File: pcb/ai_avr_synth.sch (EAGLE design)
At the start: 45 parts, among them IC1 ATMEGA328P-PDIP, J1 1X02ST, J2 1X06, J3 1X08, J4 1X08, J5 MIDIJACK, J6 STEREOJACKSJ1-3555NG, U1 MC7805, U2 TLC2262, U3 6N138

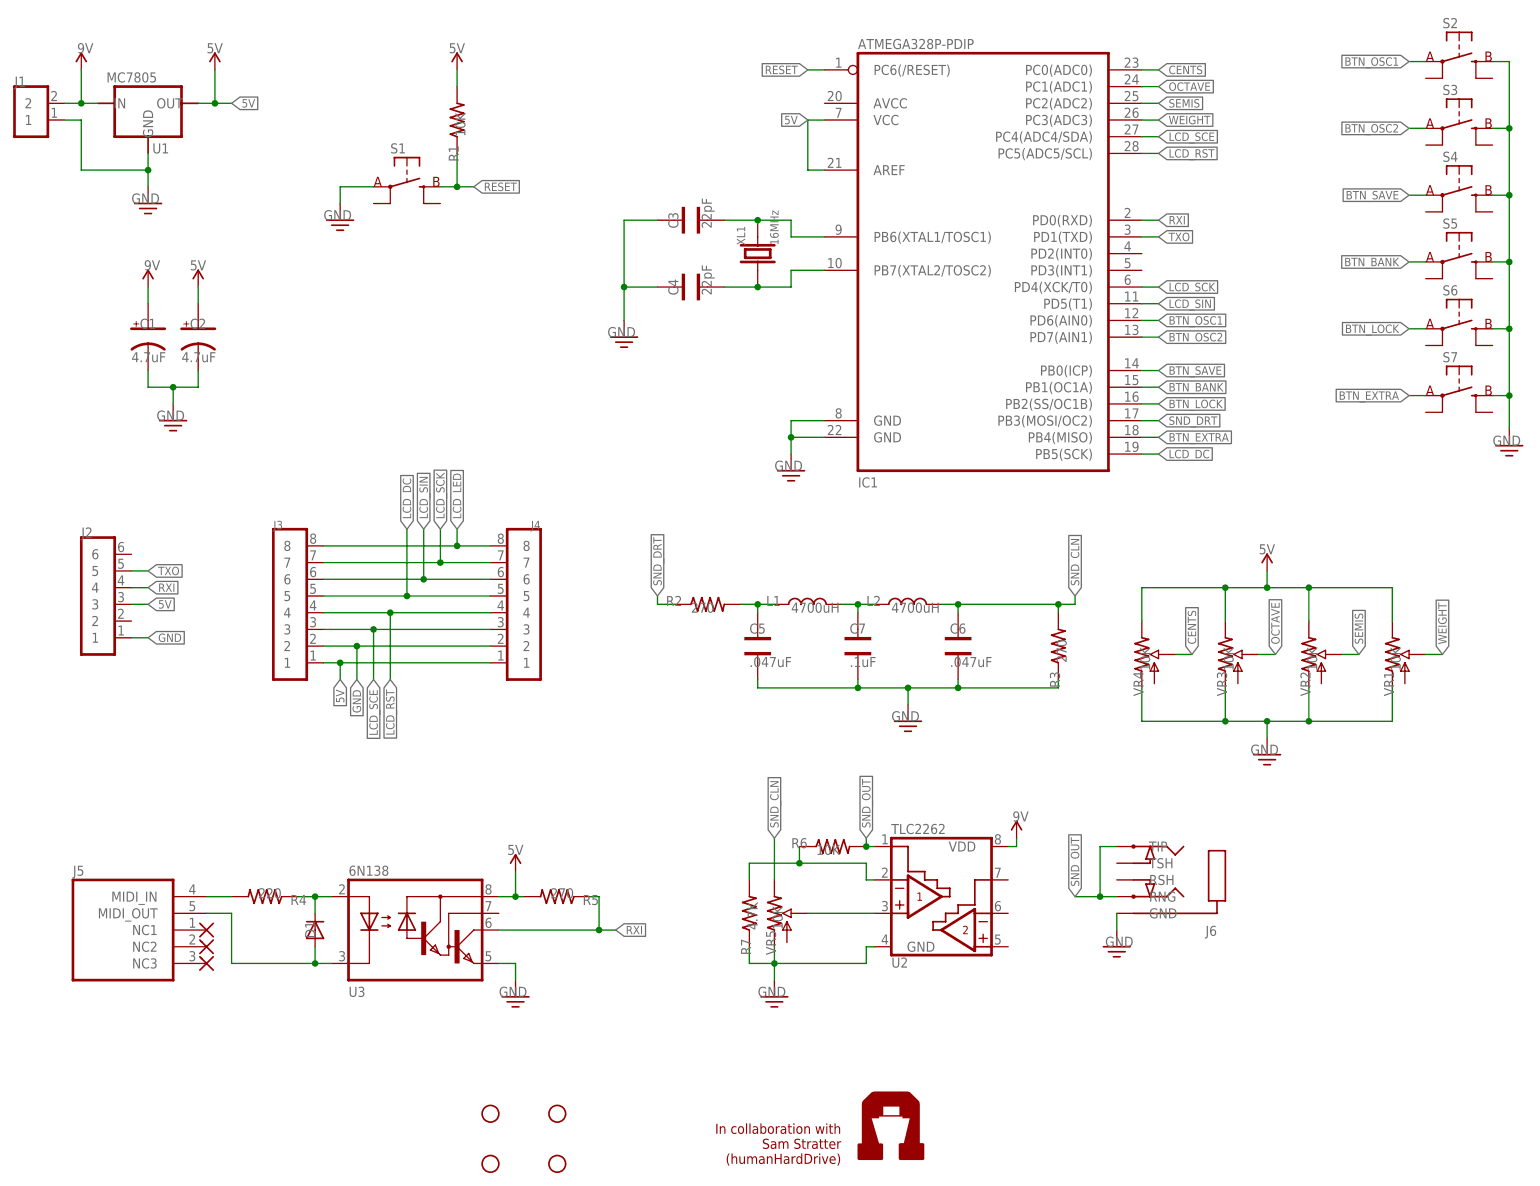
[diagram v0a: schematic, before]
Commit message: Revisions on LCD orientation, and positioning of switches/pots.
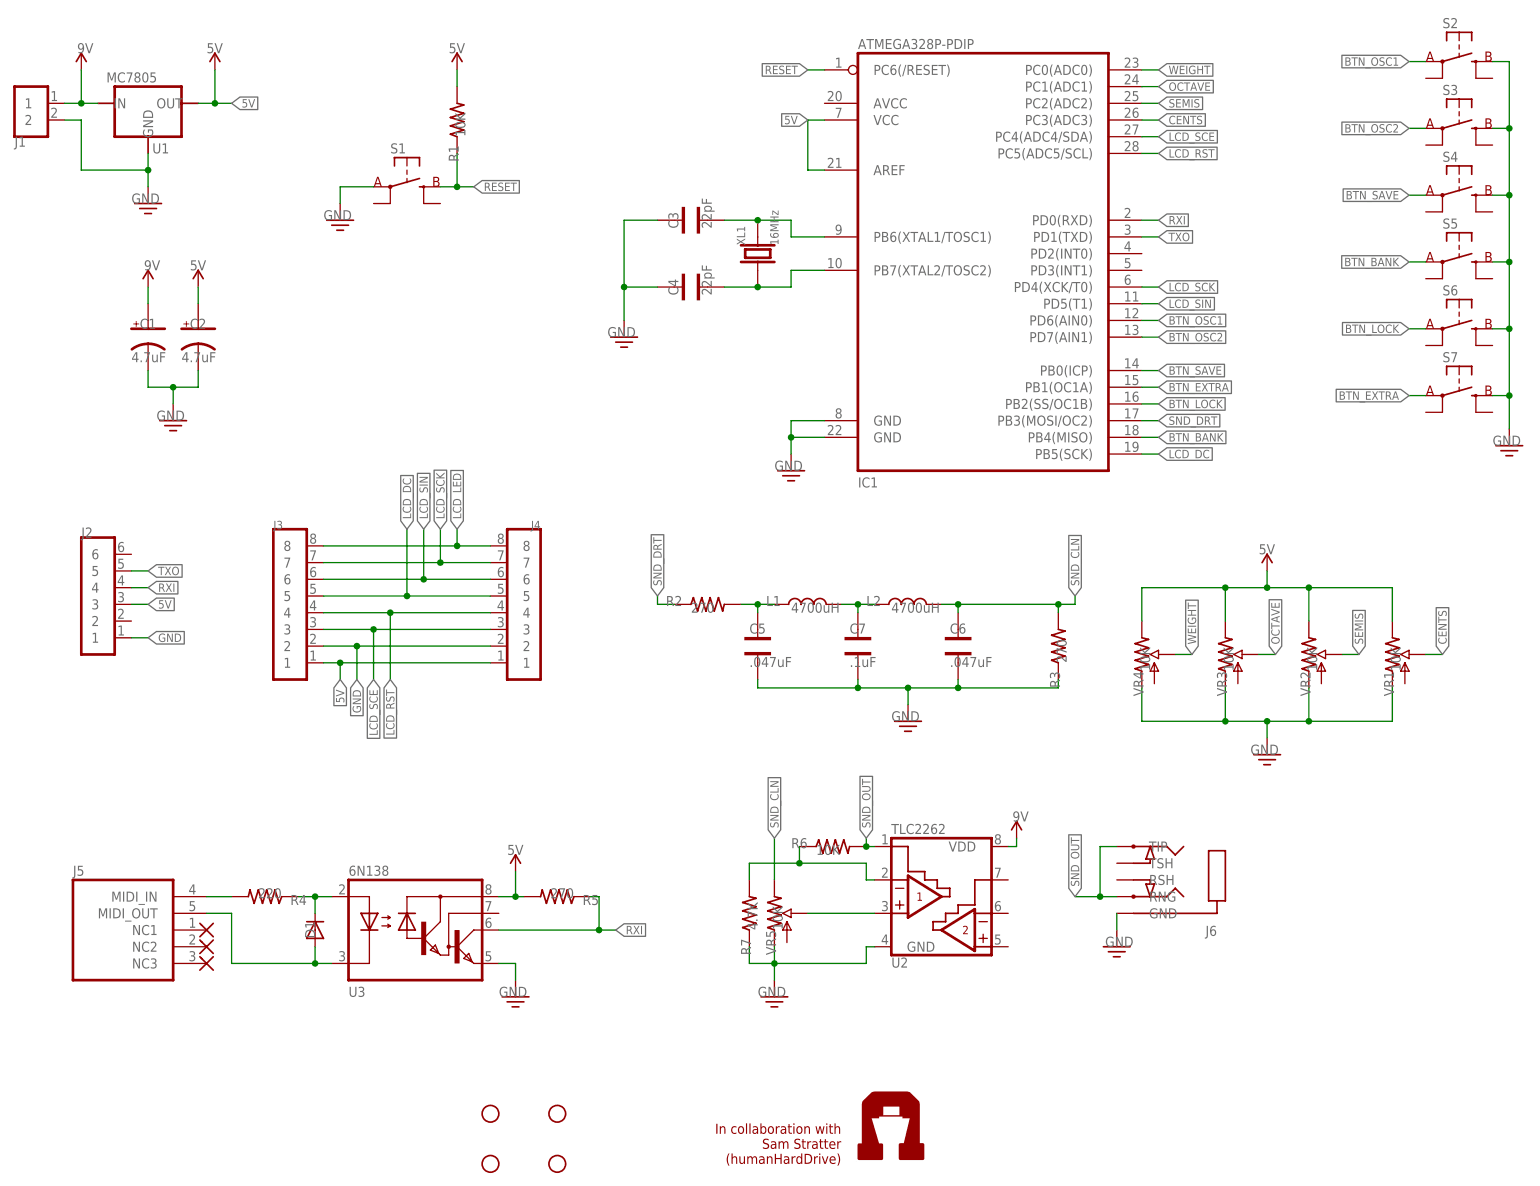
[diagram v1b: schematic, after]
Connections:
- net 9V: now also J1.1; no longer J1.2
- net BTN_BANK: now also IC1.PB4(MISO); no longer IC1.PB1(OC1A)
- net BTN_EXTRA: now also IC1.PB1(OC1A); no longer IC1.PB4(MISO)
- net CENTS: now also IC1.PC3(ADC3), VR1.S; no longer IC1.PC0(ADC0), VR4.S
- net GND: now also J1.2; no longer J1.1
- net WEIGHT: now also IC1.PC0(ADC0), VR4.S; no longer IC1.PC3(ADC3), VR1.S
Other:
- moved on the sheet: J1
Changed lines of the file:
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@@
 </variantdefs>
 <classes>
-<class number="0" name="default" width="0" drill="0">
+<class number="0" name="default" width="0.4064" drill="0">
+</class>
+<class number="1" name="PWR" width="0.6096" drill="0">
 </class>
 </classes>
@@
 <instance part="C1" gate="G$1" x="26.67" y="130.81"/>
 <instance part="C2" gate="G$1" x="34.29" y="130.81"/>
-<instance part="J1" gate="G$1" x="8.89" y="166.37"/>
+<instance part="J1" gate="G$1" x="8.89" y="163.83" rot="MR180"/>
 <instance part="U$1" gate="G$1" x="16.51" y="171.45"/>
 <instance part="GND1" gate="GND" x="26.67" y="151.13"/>
@@
 <pinref part="GND1" gate="GND" pin="GND"/>
 <wire x1="26.67" y1="153.67" x2="26.67" y2="156.21" width="0.1524" layer="91"/>
-<pinref part="J1" gate="G$1" pin="1"/>
 <wire x1="26.67" y1="156.21" x2="26.67" y2="158.75" width="0.1524" layer="91"/>
+<wire x1="16.51" y1="156.21" x2="26.67" y2="156.21" width="0.1524" layer="91"/>
+<junction x="26.67" y="156.21"/>
+<pinref part="J1" gate="G$1" pin="2"/>
 <wire x1="13.97" y1="163.83" x2="16.51" y2="163.83" width="0.1524" layer="91"/>
 <wire x1="16.51" y1="163.83" x2="16.51" y2="156.21" width="0.1524" layer="91"/>
-<wire x1="16.51" y1="156.21" x2="26.67" y2="156.21" width="0.1524" layer="91"/>
-<junction x="26.67" y="156.21"/>
 </segment>
 <segment>
@@
 </segment>
 </net>
-<net name="9V" class="0">
-<segment>
-<pinref part="J1" gate="G$1" pin="2"/>
+<net name="9V" class="1">
+<segment>
 <pinref part="U1" gate="G$1" pin="IN"/>
-<wire x1="13.97" y1="166.37" x2="16.51" y2="166.37" width="0.1524" layer="91"/>
 <pinref part="U$1" gate="G$1" pin="9V"/>
 <wire x1="16.51" y1="166.37" x2="19.05" y2="166.37" width="0.1524" layer="91"/>
 <wire x1="16.51" y1="171.45" x2="16.51" y2="166.37" width="0.1524" layer="91"/>
+<pinref part="J1" gate="G$1" pin="1"/>
+<wire x1="13.97" y1="166.37" x2="16.51" y2="166.37" width="0.1524" layer="91"/>
 <junction x="16.51" y="166.37"/>
 </segment>
@@
 </segment>
 </net>
-<net name="5V" class="0">
+<net name="5V" class="1">
 <segment>
 <pinref part="U1" gate="G$1" pin="OUT"/>
@@
 <net name="CENTS" class="0">
 <segment>
+<pinref part="IC1" gate="G$1" pin="PC3(ADC3)"/>
+<wire x1="177.8" y1="163.83" x2="180.34" y2="163.83" width="0.1524" layer="91"/>
+<label x="180.34" y="163.83" size="1.27" layer="95" ratio="15" xref="yes"/>
+</segment>
+<segment>
+<pinref part="VR1" gate="G$1" pin="S"/>
+<wire x1="220.98" y1="82.55" x2="223.52" y2="82.55" width="0.1524" layer="91"/>
+<label x="223.52" y="82.55" size="1.27" layer="95" ratio="15" rot="R90" xref="yes"/>
+</segment>
+</net>
+<net name="OCTAVE" class="0">
+<segment>
+<pinref part="IC1" gate="G$1" pin="PC1(ADC1)"/>
+<wire x1="177.8" y1="168.91" x2="180.34" y2="168.91" width="0.1524" layer="91"/>
+<label x="180.34" y="168.91" size="1.27" layer="95" ratio="15" xref="yes"/>
+</segment>
+<segment>
+<pinref part="VR3" gate="G$1" pin="S"/>
+<wire x1="195.58" y1="82.55" x2="198.12" y2="82.55" width="0.1524" layer="91"/>
+<label x="198.12" y="82.55" size="1.27" layer="95" ratio="15" rot="R90" xref="yes"/>
+</segment>
+</net>
+<net name="SEMIS" class="0">
+<segment>
+<pinref part="IC1" gate="G$1" pin="PC2(ADC2)"/>
+<wire x1="177.8" y1="166.37" x2="180.34" y2="166.37" width="0.1524" layer="91"/>
+<label x="180.34" y="166.37" size="1.27" layer="95" ratio="15" xref="yes"/>
+</segment>
+<segment>
+<pinref part="VR2" gate="G$1" pin="S"/>
+<wire x1="208.28" y1="82.55" x2="210.82" y2="82.55" width="0.1524" layer="91"/>
+<label x="210.82" y="82.55" size="1.27" layer="95" ratio="15" rot="R90" xref="yes"/>
+</segment>
+</net>
+<net name="WEIGHT" class="0">
+<segment>
 <pinref part="IC1" gate="G$1" pin="PC0(ADC0)"/>
 <wire x1="177.8" y1="171.45" x2="180.34" y2="171.45" width="0.1524" layer="91"/>
@@
 <wire x1="182.88" y1="82.55" x2="185.42" y2="82.55" width="0.1524" layer="91"/>
 <label x="185.42" y="82.55" size="1.27" layer="95" ratio="15" rot="R90" xref="yes"/>
-</segment>
-</net>
-<net name="OCTAVE" class="0">
-<segment>
-<pinref part="IC1" gate="G$1" pin="PC1(ADC1)"/>
-<wire x1="177.8" y1="168.91" x2="180.34" y2="168.91" width="0.1524" layer="91"/>
-<label x="180.34" y="168.91" size="1.27" layer="95" ratio="15" xref="yes"/>
-</segment>
-<segment>
-<pinref part="VR3" gate="G$1" pin="S"/>
-<wire x1="195.58" y1="82.55" x2="198.12" y2="82.55" width="0.1524" layer="91"/>
-<label x="198.12" y="82.55" size="1.27" layer="95" ratio="15" rot="R90" xref="yes"/>
-</segment>
-</net>
-<net name="SEMIS" class="0">
-<segment>
-<pinref part="IC1" gate="G$1" pin="PC2(ADC2)"/>
-<wire x1="177.8" y1="166.37" x2="180.34" y2="166.37" width="0.1524" layer="91"/>
-<label x="180.34" y="166.37" size="1.27" layer="95" ratio="15" xref="yes"/>
-</segment>
-<segment>
-<pinref part="VR2" gate="G$1" pin="S"/>
-<wire x1="208.28" y1="82.55" x2="210.82" y2="82.55" width="0.1524" layer="91"/>
-<label x="210.82" y="82.55" size="1.27" layer="95" ratio="15" rot="R90" xref="yes"/>
-</segment>
-</net>
-<net name="WEIGHT" class="0">
-<segment>
-<pinref part="IC1" gate="G$1" pin="PC3(ADC3)"/>
-<wire x1="177.8" y1="163.83" x2="180.34" y2="163.83" width="0.1524" layer="91"/>
-<label x="180.34" y="163.83" size="1.27" layer="95" ratio="15" xref="yes"/>
-</segment>
-<segment>
-<pinref part="VR1" gate="G$1" pin="S"/>
-<wire x1="220.98" y1="82.55" x2="223.52" y2="82.55" width="0.1524" layer="91"/>
-<label x="223.52" y="82.55" size="1.27" layer="95" ratio="15" rot="R90" xref="yes"/>
 </segment>
 </net>
@@
 <net name="BTN_BANK" class="0">
 <segment>
-<pinref part="IC1" gate="G$1" pin="PB1(OC1A)"/>
-<wire x1="177.8" y1="123.19" x2="180.34" y2="123.19" width="0.1524" layer="91"/>
-<label x="180.34" y="123.19" size="1.27" layer="95" ratio="15" xref="yes"/>
-</segment>
-<segment>
 <pinref part="S5" gate="G$1" pin="A@1"/>
 <wire x1="220.98" y1="142.24" x2="218.44" y2="142.24" width="0.1524" layer="91"/>
 <label x="218.44" y="142.24" size="1.27" layer="95" ratio="15" rot="R180" xref="yes"/>
+</segment>
+<segment>
+<pinref part="IC1" gate="G$1" pin="PB4(MISO)"/>
+<wire x1="177.8" y1="115.57" x2="180.34" y2="115.57" width="0.1524" layer="91"/>
+<label x="180.34" y="115.57" size="1.27" layer="95" ratio="15" xref="yes"/>
 </segment>
 </net>
@@
 <net name="BTN_EXTRA" class="0">
 <segment>
-<pinref part="IC1" gate="G$1" pin="PB4(MISO)"/>
-<wire x1="177.8" y1="115.57" x2="180.34" y2="115.57" width="0.1524" layer="91"/>
-<label x="180.34" y="115.57" size="1.27" layer="95" ratio="15" xref="yes"/>
-</segment>
-<segment>
 <pinref part="S7" gate="G$1" pin="A@1"/>
 <wire x1="220.98" y1="121.92" x2="218.44" y2="121.92" width="0.1524" layer="91"/>
 <label x="218.44" y="121.92" size="1.27" layer="95" ratio="15" rot="R180" xref="yes"/>
 </segment>
-</net>
+<segment>
+<pinref part="IC1" gate="G$1" pin="PB1(OC1A)"/>
+<wire x1="177.8" y1="123.19" x2="180.34" y2="123.19" width="0.1524" layer="91"/>
+<label x="180.34" y="123.19" size="1.27" layer="95" ratio="15" xref="yes"/>
+</segment>
+</net>

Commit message: Adding gerbers, firmware. Updated README and index.
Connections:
- removed net N$2: C3.2, IC1.PB6(XTAL1/TOSC1), XL1.2
- removed net N$8: J5.MIDI_IN, R4.2
- new net N$1: J5.MIDI_IN, R4.1
- new net N$4: C3.1, IC1.PB6(XTAL1/TOSC1), XL1.2
- net 5V: now also R5.1; no longer R5.2
- net GND: now also C3.2, C4.2; no longer C3.1, C4.1
- net N$3: now also C4.1; no longer C4.2
- net N$9: now also R4.2; no longer R4.1
- net RXI: now also R5.2; no longer R5.1
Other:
- moved on the sheet: C3, C4, R4, R5
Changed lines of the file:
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@@
 <setting verticaltext="up"/>
 </settings>
-<grid distance="50" unitdist="mil" unit="mil" style="lines" multiple="1" display="yes" altdistance="0.01" altunitdist="inch" altunit="inch"/>
+<grid distance="25" unitdist="mil" unit="mil" style="lines" multiple="1" display="yes" altdistance="0.01" altunitdist="inch" altunit="inch"/>
 <layers>
 <layer number="1" name="Top" color="4" fill="1" visible="no" active="no"/>
@@
 <instance part="STANDOFF8" gate="G$1" x="88.9" y="12.7"/>
 <instance part="XL1" gate="G$1" x="119.38" y="143.51" rot="R90"/>
-<instance part="C3" gate="G$1" x="109.22" y="148.59" rot="R90"/>
-<instance part="C4" gate="G$1" x="109.22" y="138.43" rot="R90"/>
+<instance part="C3" gate="G$1" x="109.22" y="148.59" rot="R270"/>
+<instance part="C4" gate="G$1" x="109.22" y="138.43" rot="R270"/>
 <instance part="C5" gate="G$1" x="119.38" y="83.82"/>
 <instance part="C6" gate="G$1" x="149.86" y="83.82"/>
 <instance part="C7" gate="G$1" x="134.62" y="83.82"/>
-<instance part="R5" gate="G$1" x="88.9" y="45.72" rot="R180"/>
+<instance part="R5" gate="G$1" x="88.9" y="45.72"/>
 <instance part="R2" gate="G$1" x="111.76" y="90.17"/>
 <instance part="R3" gate="G$1" x="165.1" y="83.82" rot="R90"/>
-<instance part="R4" gate="G$1" x="44.45" y="45.72" rot="R180"/>
+<instance part="R4" gate="G$1" x="44.45" y="45.72"/>
 <instance part="R1" gate="G$1" x="73.66" y="163.83" rot="R90"/>
 <instance part="R6" gate="G$1" x="130.81" y="53.34"/>
@@
 </segment>
 <segment>
-<pinref part="C3" gate="G$1" pin="1"/>
+<wire x1="99.06" y1="148.59" x2="99.06" y2="138.43" width="0.1524" layer="91"/>
+<pinref part="GND4" gate="GND" pin="GND"/>
+<pinref part="C3" gate="G$1" pin="2"/>
+<wire x1="99.06" y1="138.43" x2="99.06" y2="133.35" width="0.1524" layer="91"/>
 <wire x1="104.14" y1="148.59" x2="99.06" y2="148.59" width="0.1524" layer="91"/>
-<wire x1="99.06" y1="148.59" x2="99.06" y2="138.43" width="0.1524" layer="91"/>
-<pinref part="C4" gate="G$1" pin="1"/>
-<wire x1="99.06" y1="138.43" x2="99.06" y2="133.35" width="0.1524" layer="91"/>
-<wire x1="99.06" y1="138.43" x2="104.14" y2="138.43" width="0.1524" layer="91"/>
+<pinref part="C4" gate="G$1" pin="2"/>
+<wire x1="104.14" y1="138.43" x2="99.06" y2="138.43" width="0.1524" layer="91"/>
 <junction x="99.06" y="138.43"/>
-<pinref part="GND4" gate="GND" pin="GND"/>
 </segment>
 <segment>
@@
 <segment>
 <pinref part="U3" gate="G$1" pin="VCC"/>
-<pinref part="R5" gate="G$1" pin="2"/>
 <wire x1="80.01" y1="45.72" x2="82.55" y2="45.72" width="0.1524" layer="91"/>
+<wire x1="82.55" y1="45.72" x2="82.55" y2="49.53" width="0.1524" layer="91"/>
+<pinref part="U$8" gate="G$1" pin="5V"/>
+<pinref part="R5" gate="G$1" pin="1"/>
 <wire x1="82.55" y1="45.72" x2="83.82" y2="45.72" width="0.1524" layer="91"/>
-<wire x1="82.55" y1="45.72" x2="82.55" y2="49.53" width="0.1524" layer="91"/>
 <junction x="82.55" y="45.72"/>
-<pinref part="U$8" gate="G$1" pin="5V"/>
 </segment>
 <segment>
@@
 </segment>
 </net>
-<net name="N$2" class="0">
-<segment>
-<pinref part="XL1" gate="G$1" pin="2"/>
-<wire x1="119.38" y1="148.59" x2="124.46" y2="148.59" width="0.1524" layer="91"/>
-<wire x1="124.46" y1="148.59" x2="124.46" y2="146.05" width="0.1524" layer="91"/>
-<pinref part="IC1" gate="G$1" pin="PB6(XTAL1/TOSC1)"/>
-<wire x1="124.46" y1="146.05" x2="129.54" y2="146.05" width="0.1524" layer="91"/>
-<pinref part="C3" gate="G$1" pin="2"/>
-<wire x1="114.3" y1="148.59" x2="119.38" y2="148.59" width="0.1524" layer="91"/>
-<junction x="119.38" y="148.59"/>
-</segment>
-</net>
 <net name="N$3" class="0">
 <segment>
@@
 <pinref part="IC1" gate="G$1" pin="PB7(XTAL2/TOSC2)"/>
 <wire x1="124.46" y1="140.97" x2="129.54" y2="140.97" width="0.1524" layer="91"/>
-<pinref part="C4" gate="G$1" pin="2"/>
+<pinref part="C4" gate="G$1" pin="1"/>
 <wire x1="114.3" y1="138.43" x2="119.38" y2="138.43" width="0.1524" layer="91"/>
 <junction x="119.38" y="138.43"/>
@@
 <wire x1="80.01" y1="40.64" x2="95.25" y2="40.64" width="0.1524" layer="91"/>
 <label x="97.79" y="40.64" size="1.27" layer="95" ratio="15" xref="yes"/>
-<pinref part="R5" gate="G$1" pin="1"/>
 <wire x1="95.25" y1="40.64" x2="97.79" y2="40.64" width="0.1524" layer="91"/>
-<wire x1="93.98" y1="45.72" x2="95.25" y2="45.72" width="0.1524" layer="91"/>
 <wire x1="95.25" y1="45.72" x2="95.25" y2="40.64" width="0.1524" layer="91"/>
 <junction x="95.25" y="40.64"/>
+<pinref part="R5" gate="G$1" pin="2"/>
+<wire x1="93.98" y1="45.72" x2="95.25" y2="45.72" width="0.1524" layer="91"/>
 </segment>
 <segment>
@@
 </segment>
 </net>
-<net name="N$8" class="0">
-<segment>
-<pinref part="J5" gate="G$1" pin="MIDI_IN"/>
-<pinref part="R4" gate="G$1" pin="2"/>
-<wire x1="35.56" y1="45.72" x2="39.37" y2="45.72" width="0.1524" layer="91"/>
-</segment>
-</net>
 <net name="N$9" class="0">
 <segment>
-<pinref part="R4" gate="G$1" pin="1"/>
-<wire x1="49.53" y1="45.72" x2="52.07" y2="45.72" width="0.1524" layer="91"/>
 <pinref part="D1" gate="G$1" pin="C"/>
 <wire x1="52.07" y1="45.72" x2="52.07" y2="43.18" width="0.1524" layer="91"/>
 <pinref part="U3" gate="G$1" pin="A"/>
 <wire x1="52.07" y1="45.72" x2="54.61" y2="45.72" width="0.1524" layer="91"/>
+<pinref part="R4" gate="G$1" pin="2"/>
+<wire x1="49.53" y1="45.72" x2="52.07" y2="45.72" width="0.1524" layer="91"/>
 <junction x="52.07" y="45.72"/>
 </segment>
@@
 </segment>
 </net>
+<net name="N$1" class="0">
+<segment>
+<pinref part="J5" gate="G$1" pin="MIDI_IN"/>
+<pinref part="R4" gate="G$1" pin="1"/>
+<wire x1="35.56" y1="45.72" x2="39.37" y2="45.72" width="0.1524" layer="91"/>
+</segment>
+</net>
+<net name="N$4" class="0">
+<segment>
+<pinref part="C3" gate="G$1" pin="1"/>
+<pinref part="XL1" gate="G$1" pin="2"/>
+<wire x1="114.3" y1="148.59" x2="119.38" y2="148.59" width="0.1524" layer="91"/>
+<wire x1="124.46" y1="148.59" x2="124.46" y2="146.05" width="0.1524" layer="91"/>
+<pinref part="IC1" gate="G$1" pin="PB6(XTAL1/TOSC1)"/>
+<wire x1="124.46" y1="146.05" x2="129.54" y2="146.05" width="0.1524" layer="91"/>
+<wire x1="119.38" y1="148.59" x2="124.46" y2="148.59" width="0.1524" layer="91"/>
+<junction x="119.38" y="148.59"/>
+</segment>
+</net>
